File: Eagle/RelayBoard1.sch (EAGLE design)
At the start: 12 parts, among them IC1 ULN2003AN, K1 4052, K2 4052, K3 4052, X1 MKDSN1,5/6-5,08, X2 MKDSN1,5/6-5,08, X4 MKDSN1,5/3-5,08, X5 MKDSN1,5/4-5,08, X6 MKDSN1,5/2-5,08

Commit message: - present working state
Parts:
- removed SV1: (no value), con-lsta:FE05-1
- removed SV2: (no value), con-lsta:FE09-1
- removed X4: MKDSN1,5/3-5,08, con-phoenix-508:MKDSN1,5/3-5,08
- added X3: Con1, con-molex:KK-156-9
- added X7: Con2, con-molex:KK-156-5
- added X8, X9: (no value), con-molex:KK-156-3
- C1: value (none) -> 100nF
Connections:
- new net N$27: IC1.O6, X8-3.S
- new net N$28: IC1.O7, X8-2.S
- new net N$29: IC1.O4, X9-3.S
- new net N$30: IC1.O5, X9-2.S
- net +12V: now also X7-1.S, X7-2.S; no longer SV1.4, SV1.5
- net +5V: now also X3-1.S, X7-3.S; no longer SV1.3, SV2.1
- net 0V: now also X3-9.S, X7-4.S, X7-5.S, X8-1.S, X9-1.S; no longer SV1.1, SV1.2, SV2.9
- net N$18: now also X3-2.S; no longer SV2.2
- net N$19: now also X3-3.S; no longer SV2.3
- net N$20: now also X3-4.S; no longer SV2.4
- net N$21: now also X3-5.S; no longer SV2.5
- net N$22: now also X3-6.S; no longer SV2.6
- net N$23: now also X3-7.S; no longer SV2.7
- net N$24: now also X3-8.S; no longer SV2.8

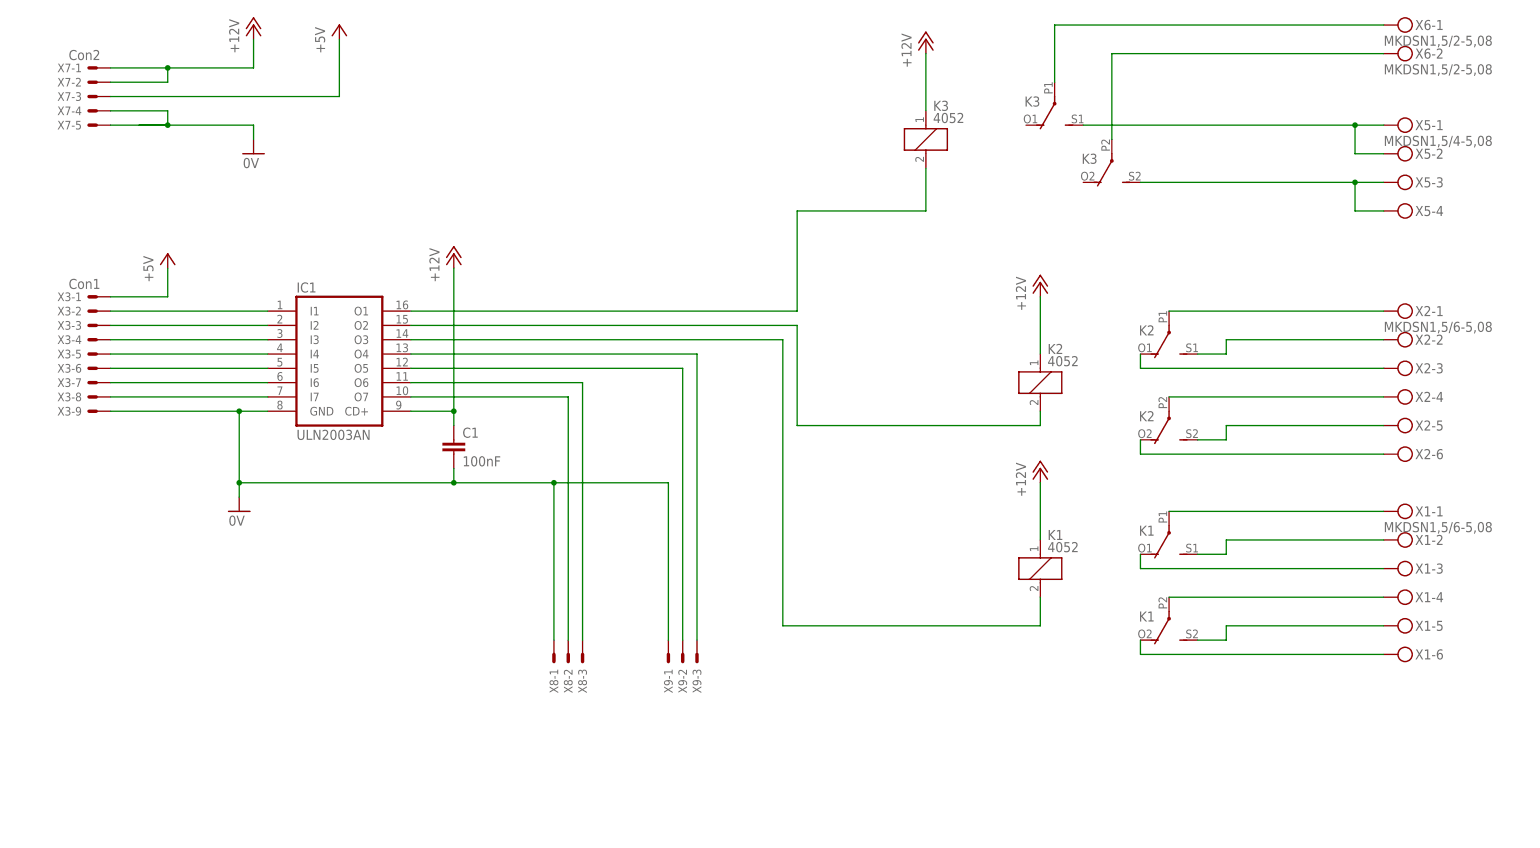
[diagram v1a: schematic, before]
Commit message: - more boards added
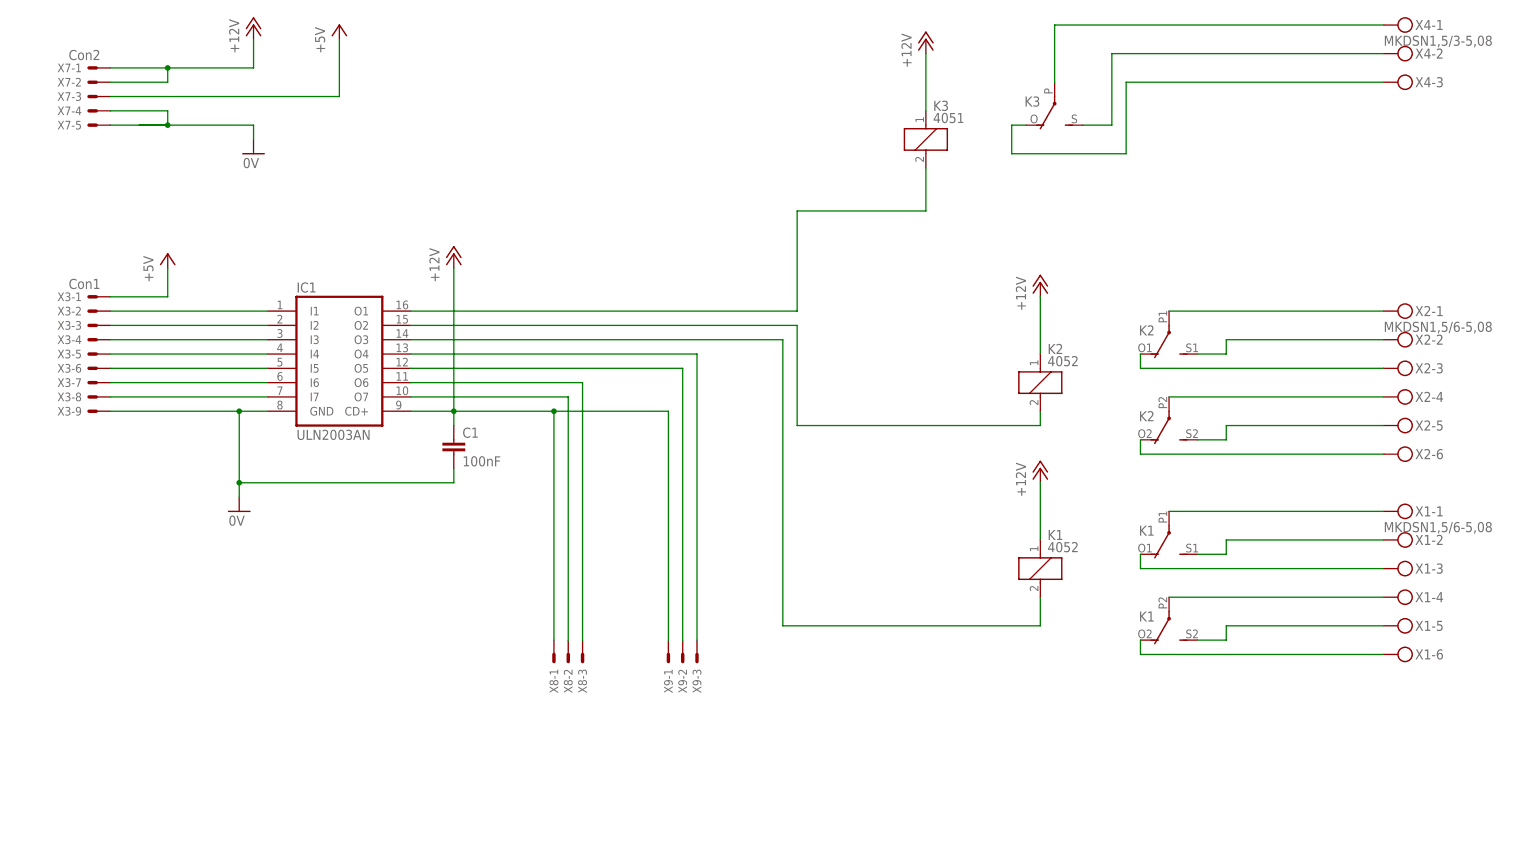
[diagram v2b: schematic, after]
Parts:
- removed X5: MKDSN1,5/4-5,08, con-phoenix-508:MKDSN1,5/4-5,08
- removed X6: MKDSN1,5/2-5,08, con-phoenix-508:MKDSN1,5/2-5,08
- added X4: MKDSN1,5/3-5,08, con-phoenix-508:MKDSN1,5/3-5,08
- K3: value 4052 -> 4051; device relay:4052 -> relay:G2R; OC_FARNELL (none) -> 1569185
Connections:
- removed net N$5: K33.S, X5-3.KL, X5-4.KL
- net +12V: now also X8-1.S, X9-1.S
- net 0V: no longer X8-1.S, X9-1.S
- net N$1: now also X4-1.KL; no longer X6-1.KL
- net N$2: now also K32.S, X4-2.KL; no longer K33.P, X6-2.KL
- net N$3: now also K32.O, X4-3.KL; no longer K32.S, X5-1.KL, X5-2.KL
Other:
- moved on the sheet: K3
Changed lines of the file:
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@@
 <part name="K1" library="relay" deviceset="4052" device=""/>
 <part name="K2" library="relay" deviceset="4052" device=""/>
-<part name="K3" library="relay" deviceset="4052" device=""/>
+<part name="K3" library="relay" deviceset="G2R" device="" value="4051">
+<attribute name="OC_FARNELL" value="1569185"/>
+</part>
 <part name="X1" library="con-phoenix-508" deviceset="MKDSN1,5/6-5,08" device=""/>
 <part name="X2" library="con-phoenix-508" deviceset="MKDSN1,5/6-5,08" device=""/>
-<part name="X5" library="con-phoenix-508" deviceset="MKDSN1,5/4-5,08" device=""/>
-<part name="X6" library="con-phoenix-508" deviceset="MKDSN1,5/2-5,08" device=""/>
 <part name="C1" library="resistor" deviceset="C-EU" device="025-025X050" value="100nF"/>
 <part name="P+1" library="supply1" deviceset="+12V" device=""/>
@@
 <part name="X8" library="con-molex" deviceset="KK-156-3" device=""/>
 <part name="X9" library="con-molex" deviceset="KK-156-3" device=""/>
+<part name="X4" library="con-phoenix-508" deviceset="MKDSN1,5/3-5,08" device="">
+<attribute name="MPN" value="SMKDSN1,5/3-5,08"/>
+<attribute name="OC_FARNELL" value="1792904"/>
+<attribute name="OC_NEWARK" value="70R0299"/>
+</part>
 </parts>
 <sheets>
@@
 <instance part="K3" gate="1" x="162.56" y="149.86"/>
 <instance part="K3" gate="2" x="185.42" y="157.48" rot="R180"/>
-<instance part="K3" gate="3" x="195.58" y="147.32" rot="R180"/>
 <instance part="X1" gate="-1" x="246.38" y="83.82"/>
 <instance part="X1" gate="-2" x="246.38" y="78.74"/>
@@
 <instance part="X2" gate="-5" x="246.38" y="99.06"/>
 <instance part="X2" gate="-6" x="246.38" y="93.98"/>
-<instance part="X5" gate="-1" x="246.38" y="152.4"/>
-<instance part="X5" gate="-2" x="246.38" y="147.32"/>
-<instance part="X5" gate="-3" x="246.38" y="142.24"/>
-<instance part="X5" gate="-4" x="246.38" y="137.16"/>
-<instance part="X6" gate="-1" x="246.38" y="170.18"/>
-<instance part="X6" gate="-2" x="246.38" y="165.1"/>
 <instance part="C1" gate="G$1" x="78.74" y="96.52"/>
 <instance part="P+1" gate="1" x="43.18" y="170.18"/>
@@
 <instance part="X9" gate="-2" x="119.38" y="58.42" rot="R270"/>
 <instance part="X9" gate="-3" x="121.92" y="58.42" rot="R270"/>
+<instance part="X4" gate="-1" x="246.38" y="170.18"/>
+<instance part="X4" gate="-2" x="246.38" y="165.1"/>
+<instance part="X4" gate="-3" x="246.38" y="160.02"/>
 </instances>
 <busses>
@@
 <net name="N$1" class="0">
 <segment>
-<pinref part="X6" gate="-1" pin="KL"/>
 <wire x1="243.84" y1="170.18" x2="185.42" y2="170.18" width="0.1524" layer="91"/>
 <pinref part="K3" gate="2" pin="P"/>
 <wire x1="185.42" y1="170.18" x2="185.42" y2="160.02" width="0.1524" layer="91"/>
+<pinref part="X4" gate="-1" pin="KL"/>
 </segment>
 </net>
 <net name="N$2" class="0">
 <segment>
-<pinref part="X6" gate="-2" pin="KL"/>
 <wire x1="243.84" y1="165.1" x2="195.58" y2="165.1" width="0.1524" layer="91"/>
-<pinref part="K3" gate="3" pin="P"/>
-<wire x1="195.58" y1="165.1" x2="195.58" y2="149.86" width="0.1524" layer="91"/>
-</segment>
-</net>
-<net name="N$3" class="0">
-<segment>
+<wire x1="195.58" y1="165.1" x2="195.58" y2="152.4" width="0.1524" layer="91"/>
 <pinref part="K3" gate="2" pin="S"/>
-<pinref part="X5" gate="-1" pin="KL"/>
-<wire x1="190.5" y1="152.4" x2="238.76" y2="152.4" width="0.1524" layer="91"/>
-<pinref part="X5" gate="-2" pin="KL"/>
-<wire x1="238.76" y1="152.4" x2="243.84" y2="152.4" width="0.1524" layer="91"/>
-<wire x1="243.84" y1="147.32" x2="238.76" y2="147.32" width="0.1524" layer="91"/>
-<wire x1="238.76" y1="147.32" x2="238.76" y2="152.4" width="0.1524" layer="91"/>
-<junction x="238.76" y="152.4"/>
-</segment>
-</net>
-<net name="N$5" class="0">
-<segment>
-<pinref part="K3" gate="3" pin="S"/>
-<pinref part="X5" gate="-3" pin="KL"/>
-<wire x1="200.66" y1="142.24" x2="238.76" y2="142.24" width="0.1524" layer="91"/>
-<wire x1="238.76" y1="142.24" x2="243.84" y2="142.24" width="0.1524" layer="91"/>
-<wire x1="238.76" y1="142.24" x2="238.76" y2="137.16" width="0.1524" layer="91"/>
-<pinref part="X5" gate="-4" pin="KL"/>
-<wire x1="238.76" y1="137.16" x2="243.84" y2="137.16" width="0.1524" layer="91"/>
-<junction x="238.76" y="142.24"/>
+<wire x1="195.58" y1="152.4" x2="190.5" y2="152.4" width="0.1524" layer="91"/>
+<pinref part="X4" gate="-2" pin="KL"/>
 </segment>
 </net>
@@
 <wire x1="78.74" y1="88.9" x2="78.74" y2="91.44" width="0.1524" layer="91"/>
 <wire x1="78.74" y1="88.9" x2="40.64" y2="88.9" width="0.1524" layer="91"/>
-<junction x="78.74" y="88.9"/>
 <pinref part="IC1" gate="A" pin="GND"/>
 <wire x1="45.72" y1="101.6" x2="40.64" y2="101.6" width="0.1524" layer="91"/>
@@
 <junction x="40.64" y="101.6"/>
 <pinref part="X3" gate="-9" pin="S"/>
-<wire x1="78.74" y1="88.9" x2="96.52" y2="88.9" width="0.1524" layer="91"/>
-<pinref part="X9" gate="-1" pin="S"/>
-<wire x1="96.52" y1="88.9" x2="116.84" y2="88.9" width="0.1524" layer="91"/>
-<wire x1="116.84" y1="88.9" x2="116.84" y2="60.96" width="0.1524" layer="91"/>
-<pinref part="X8" gate="-1" pin="S"/>
-<wire x1="96.52" y1="88.9" x2="96.52" y2="60.96" width="0.1524" layer="91"/>
-<junction x="96.52" y="88.9"/>
 <pinref part="GND2" gate="1" pin="0V"/>
 <wire x1="40.64" y1="86.36" x2="40.64" y2="88.9" width="0.1524" layer="91"/>
@@
 <wire x1="78.74" y1="101.6" x2="71.12" y2="101.6" width="0.1524" layer="91"/>
 <junction x="78.74" y="101.6"/>
+<wire x1="78.74" y1="101.6" x2="96.52" y2="101.6" width="0.1524" layer="91"/>
+<pinref part="X9" gate="-1" pin="S"/>
+<wire x1="96.52" y1="101.6" x2="116.84" y2="101.6" width="0.1524" layer="91"/>
+<wire x1="116.84" y1="101.6" x2="116.84" y2="60.96" width="0.1524" layer="91"/>
+<pinref part="X8" gate="-1" pin="S"/>
+<wire x1="96.52" y1="101.6" x2="96.52" y2="60.96" width="0.1524" layer="91"/>
+<junction x="96.52" y="101.6"/>
 </segment>
 </net>
@@
 </segment>
 </net>
+<net name="N$3" class="0">
+<segment>
+<pinref part="X4" gate="-3" pin="KL"/>
+<wire x1="243.84" y1="160.02" x2="198.12" y2="160.02" width="0.1524" layer="91"/>
+<wire x1="198.12" y1="160.02" x2="198.12" y2="147.32" width="0.1524" layer="91"/>
+<wire x1="198.12" y1="147.32" x2="177.8" y2="147.32" width="0.1524" layer="91"/>
+<wire x1="177.8" y1="147.32" x2="177.8" y2="152.4" width="0.1524" layer="91"/>
+<pinref part="K3" gate="2" pin="O"/>
+<wire x1="177.8" y1="152.4" x2="180.34" y2="152.4" width="0.1524" layer="91"/>
+</segment>
+</net>

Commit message: - some modifications, corrections, ...
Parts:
- X3: value Con1 -> CON1; device con-molex:KK-156-9 -> con-molex:KK-156-8
- X7: value Con2 -> CON2
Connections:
- net +5V: no longer X3-1.S
- net 0V: now also X3-8.S; no longer X3-9.S
- net N$18: now also X3-1.S; no longer X3-2.S
- net N$19: now also X3-2.S; no longer X3-3.S
- net N$20: now also X3-3.S; no longer X3-4.S
- net N$21: now also X3-4.S; no longer X3-5.S
- net N$22: now also X3-5.S; no longer X3-6.S
- net N$23: now also X3-6.S; no longer X3-7.S
- net N$24: now also X3-7.S; no longer X3-8.S
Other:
- moved on the sheet: X3-1, X3-2, X3-3, X3-4, X3-5, X3-6, X3-7, X3-8
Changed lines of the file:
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@@
 </layers>
 <schematic xreflabel="%F%N/%S.%C%R" xrefpart="/%S.%C%R">
+<description>Main relay unit</description>
 <attributes>
 </attributes>
@@
 <part name="GND1" library="supply1" deviceset="0V" device=""/>
 <part name="GND2" library="supply1" deviceset="0V" device=""/>
-<part name="P+4" library="supply1" deviceset="+5V" device=""/>
 <part name="P+5" library="supply1" deviceset="+12V" device=""/>
 <part name="P+6" library="supply1" deviceset="+12V" device=""/>
 <part name="P+7" library="supply1" deviceset="+12V" device=""/>
 <part name="P+3" library="supply1" deviceset="+12V" device=""/>
-<part name="X3" library="con-molex" deviceset="KK-156-9" device="" value="Con1"/>
-<part name="X7" library="con-molex" deviceset="KK-156-5" device="" value="Con2"/>
+<part name="X7" library="con-molex" deviceset="KK-156-5" device="" value="CON2"/>
 <part name="X8" library="con-molex" deviceset="KK-156-3" device=""/>
 <part name="X9" library="con-molex" deviceset="KK-156-3" device=""/>
@@
 <attribute name="OC_NEWARK" value="70R0299"/>
 </part>
+<part name="X3" library="con-molex" deviceset="KK-156-8" device="" value="CON1"/>
 </parts>
 <sheets>
 <sheet>
-<description>RotorControl</description>
+<description>RotorControl - main relay board</description>
 <plain>
 </plain>
@@
 <instance part="GND1" gate="1" x="43.18" y="147.32"/>
 <instance part="GND2" gate="1" x="40.64" y="83.82"/>
-<instance part="P+4" gate="1" x="27.94" y="129.54"/>
 <instance part="P+5" gate="1" x="162.56" y="167.64"/>
 <instance part="P+6" gate="1" x="182.88" y="124.46"/>
 <instance part="P+7" gate="1" x="182.88" y="91.44"/>
 <instance part="P+3" gate="1" x="78.74" y="129.54"/>
-<instance part="X3" gate="-1" x="15.24" y="121.92" rot="MR0"/>
-<instance part="X3" gate="-2" x="15.24" y="119.38" rot="MR0"/>
-<instance part="X3" gate="-3" x="15.24" y="116.84" rot="MR0"/>
-<instance part="X3" gate="-4" x="15.24" y="114.3" rot="MR0"/>
-<instance part="X3" gate="-5" x="15.24" y="111.76" rot="MR0"/>
-<instance part="X3" gate="-6" x="15.24" y="109.22" rot="MR0"/>
-<instance part="X3" gate="-7" x="15.24" y="106.68" rot="MR0"/>
-<instance part="X3" gate="-8" x="15.24" y="104.14" rot="MR0"/>
-<instance part="X3" gate="-9" x="15.24" y="101.6" rot="MR0"/>
 <instance part="X7" gate="-1" x="15.24" y="162.56" rot="MR0"/>
 <instance part="X7" gate="-2" x="15.24" y="160.02" rot="MR0"/>
@@
 <instance part="X4" gate="-2" x="246.38" y="165.1"/>
 <instance part="X4" gate="-3" x="246.38" y="160.02"/>
+<instance part="X3" gate="-1" x="15.24" y="119.38" rot="R180"/>
+<instance part="X3" gate="-2" x="15.24" y="116.84" rot="R180"/>
+<instance part="X3" gate="-3" x="15.24" y="114.3" rot="R180"/>
+<instance part="X3" gate="-4" x="15.24" y="111.76" rot="R180"/>
+<instance part="X3" gate="-5" x="15.24" y="109.22" rot="R180"/>
+<instance part="X3" gate="-6" x="15.24" y="106.68" rot="R180"/>
+<instance part="X3" gate="-7" x="15.24" y="104.14" rot="R180"/>
+<instance part="X3" gate="-8" x="15.24" y="101.6" rot="R180"/>
 </instances>
 <busses>
@@
 </net>
 <net name="+5V" class="0">
-<segment>
-<pinref part="P+4" gate="1" pin="+5V"/>
-<wire x1="27.94" y1="121.92" x2="27.94" y2="127" width="0.1524" layer="91"/>
-<pinref part="X3" gate="-1" pin="S"/>
-<wire x1="17.78" y1="121.92" x2="27.94" y2="121.92" width="0.1524" layer="91"/>
-</segment>
 <segment>
 <wire x1="17.78" y1="157.48" x2="58.42" y2="157.48" width="0.1524" layer="91"/>
@@
 <wire x1="40.64" y1="101.6" x2="17.78" y2="101.6" width="0.1524" layer="91"/>
 <junction x="40.64" y="101.6"/>
-<pinref part="X3" gate="-9" pin="S"/>
 <pinref part="GND2" gate="1" pin="0V"/>
 <wire x1="40.64" y1="86.36" x2="40.64" y2="88.9" width="0.1524" layer="91"/>
 <junction x="40.64" y="88.9"/>
+<pinref part="X3" gate="-8" pin="S"/>
 </segment>
 </net>
@@
 <pinref part="IC1" gate="A" pin="I1"/>
 <wire x1="45.72" y1="119.38" x2="17.78" y2="119.38" width="0.1524" layer="91"/>
-<pinref part="X3" gate="-2" pin="S"/>
+<pinref part="X3" gate="-1" pin="S"/>
 </segment>
 </net>
@@
 <pinref part="IC1" gate="A" pin="I2"/>
 <wire x1="45.72" y1="116.84" x2="17.78" y2="116.84" width="0.1524" layer="91"/>
-<pinref part="X3" gate="-3" pin="S"/>
+<pinref part="X3" gate="-2" pin="S"/>
 </segment>
 </net>
@@
 <pinref part="IC1" gate="A" pin="I3"/>
 <wire x1="45.72" y1="114.3" x2="17.78" y2="114.3" width="0.1524" layer="91"/>
-<pinref part="X3" gate="-4" pin="S"/>
+<pinref part="X3" gate="-3" pin="S"/>
 </segment>
 </net>
@@
 <pinref part="IC1" gate="A" pin="I4"/>
 <wire x1="45.72" y1="111.76" x2="17.78" y2="111.76" width="0.1524" layer="91"/>
-<pinref part="X3" gate="-5" pin="S"/>
+<pinref part="X3" gate="-4" pin="S"/>
 </segment>
 </net>
@@
 <pinref part="IC1" gate="A" pin="I5"/>
 <wire x1="45.72" y1="109.22" x2="17.78" y2="109.22" width="0.1524" layer="91"/>
-<pinref part="X3" gate="-6" pin="S"/>
+<pinref part="X3" gate="-5" pin="S"/>
 </segment>
 </net>
@@
 <pinref part="IC1" gate="A" pin="I6"/>
 <wire x1="45.72" y1="106.68" x2="17.78" y2="106.68" width="0.1524" layer="91"/>
-<pinref part="X3" gate="-7" pin="S"/>
+<pinref part="X3" gate="-6" pin="S"/>
 </segment>
 </net>
@@
 <pinref part="IC1" gate="A" pin="I7"/>
 <wire x1="45.72" y1="104.14" x2="17.78" y2="104.14" width="0.1524" layer="91"/>
-<pinref part="X3" gate="-8" pin="S"/>
-</segment>
-</net>
+<pinref part="X3" gate="-7" pin="S"/>
+</segment>
+</net>
